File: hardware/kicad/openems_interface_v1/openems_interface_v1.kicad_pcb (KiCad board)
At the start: 2 copper layers, 130 x 100 mm, 0 parts

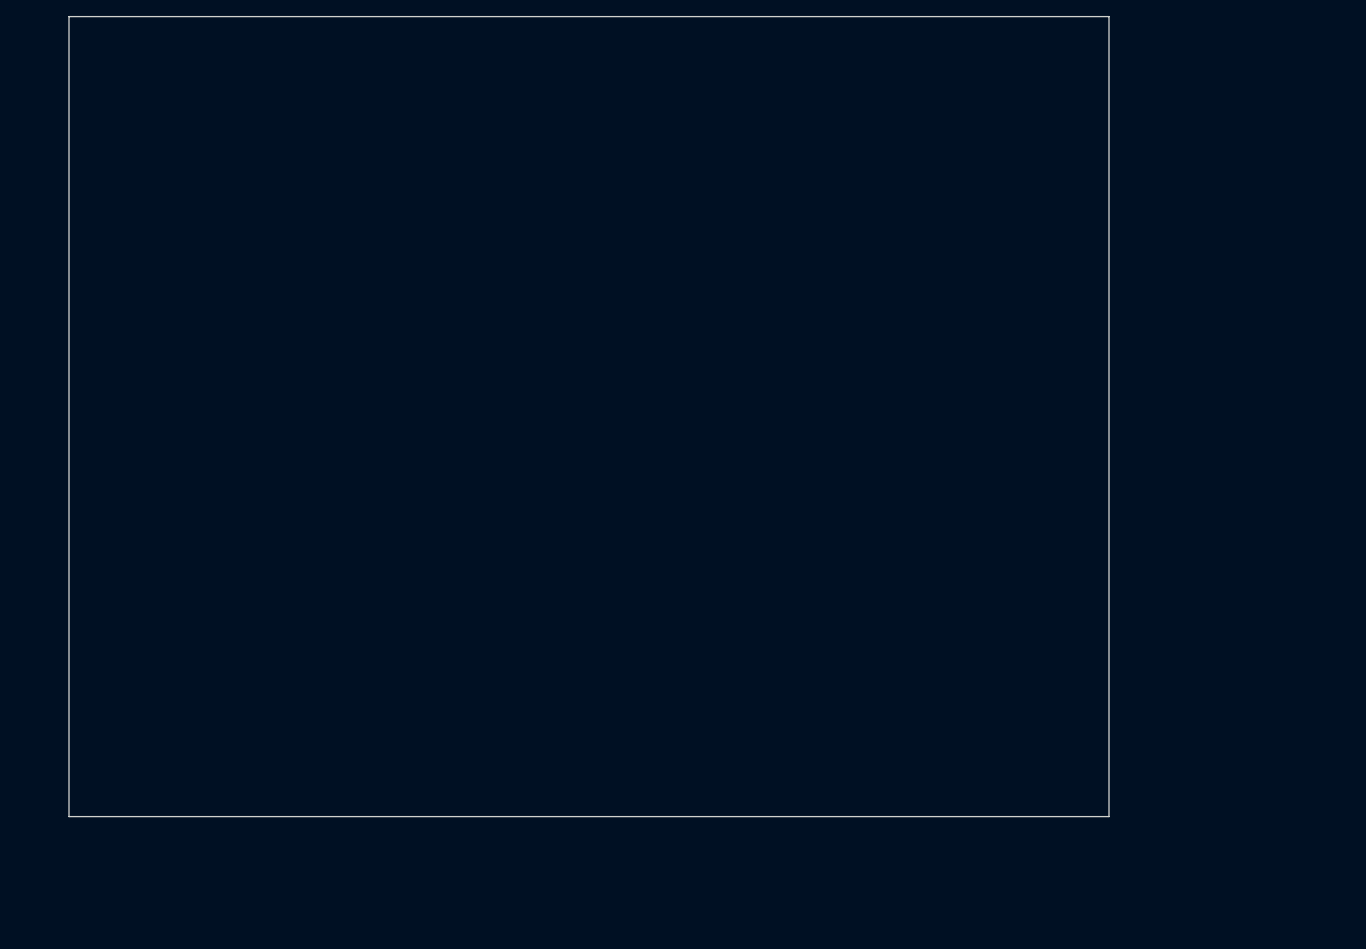
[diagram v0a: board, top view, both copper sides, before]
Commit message: feat(hw): PCB placement AMPSEAL J1/J2 + WeAct keepout
Coloca footprints TE 35/23 RA na aresta, headers 2x25 e furos M3 Φ3.2
do coreboard WeAct num outline 130x100 mm. Script build_pcb_placement.py
regenera a posição.
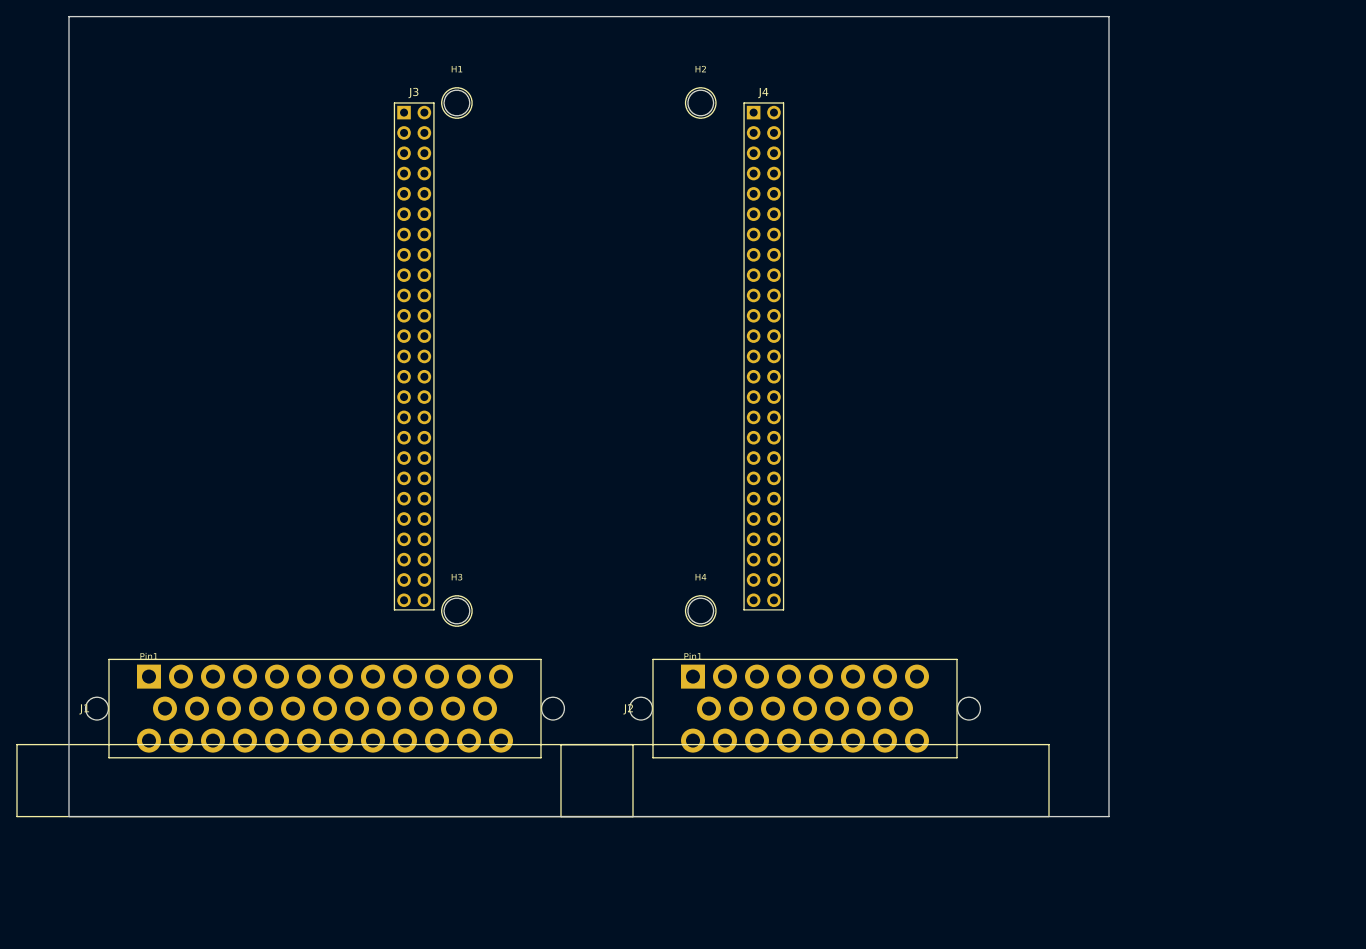
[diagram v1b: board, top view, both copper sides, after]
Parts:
- added H1: MH3.2, MountingHole:3.2mm, F.Cu at (48.5, 10.8)
- added H2: MH3.2, MountingHole:3.2mm, F.Cu at (79.0, 10.8)
- added H3: MH3.2, MountingHole:3.2mm, F.Cu at (48.5, 74.3)
- added H4: MH3.2, MountingHole:3.2mm, F.Cu at (79.0, 74.3)
- added J1: TE_776180_AMPSEAL_35_RA, OpenEMS:TE_776180_AMPSEAL_35_RA, F.Cu at (10.0, 82.5)
- added J2: TE_770669_AMPSEAL_23_RA, OpenEMS:TE_770669_AMPSEAL_23_RA, F.Cu at (78.0, 82.5)
- added J3: WeAct_PinHeader_2x25_P2.54mm, OpenEMS:WeAct_PinHeader_2x25_P2.54mm, F.Cu at (43.1, 12.0)
- added J4: WeAct_PinHeader_2x25_P2.54mm, OpenEMS:WeAct_PinHeader_2x25_P2.54mm, F.Cu at (86.9, 12.0)
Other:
- board text added: "J1 signals 1-776180-1"
- board text added: "J2 power 1-770669-1"
- board text added: "OpenEMS interface v1 — 130x100 mm\nBottom: J1 35 + J2 23 AMPSEAL RA\nCenter: WeAct 38.62x69.10 + MH Phi3.2\nNAO fabricar sem copper/GND pours"
- board text added: "WeAct keepout"
- board text removed: "J1 35-pos signals (1-776180-1)"
- board text removed: "J2 23-pos power (1-770669-1)"
- board text removed: "OpenEMS interface v1 — 130x100 mm outline Bottom edge: J1 AMPSEAL35 + gap + J2 AMPSEAL23 Center: WeAct 38.62x69.10 keepout Footprints: libs/OpenEMS.pretty — NAO fabricar ainda"
- board text removed: "WeAct keepout 38.62 x 69.10"

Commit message: feat(hw): nets J1/J2 no PCB + zones PGND + star GND no sch
Atribui pads AMPSEAL a partir de pinmap_logical.md (autoridade),
adiciona pours PGND F/B, e evita curto de terras no esquemático
(star só via NetTie no layout). Script annotate_pcb_nets.py.
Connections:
- J1 pad 1: (no net) -> CKP_P
- J1 pad 10: (no net) -> APP1
- J1 pad 11: (no net) -> APP2
- J1 pad 12: (no net) -> FUEL_PRESS
- J1 pad 13: (no net) -> OIL_PRESS
- J1 pad 14: (no net) -> ETB_TPS1
- J1 pad 15: (no net) -> ETB_TPS2
- J1 pad 16: (no net) -> +5V_SENS_A
- J1 pad 17: (no net) -> +5V_SENS_B
- J1 pad 18: (no net) -> SGND
- J1 pad 19: (no net) -> SGND
- J1 pad 2: (no net) -> CKP_N
- J1 pad 20: (no net) -> CANH
- J1 pad 21: (no net) -> CANL
- J1 pad 22: (no net) -> CAN_SHLD
- J1 pad 23: (no net) -> FLEX_12V
- J1 pad 24: (no net) -> FLEX_SIG
- J1 pad 25: (no net) -> FLEX_GND
- J1 pad 26: (no net) -> KNOCK_SIG
- J1 pad 27: (no net) -> KNOCK_SHLD
- J1 pad 28: (no net) -> CMP2_SIG
- J1 pad 29: (no net) -> CMP2_5V
- J1 pad 3: (no net) -> CKP_SHLD
- J1 pad 30: (no net) -> CMP2_GND
- J1 pad 31: (no net) -> TPS_INDEP
- J1 pad 4: (no net) -> CMP_SIG
- J1 pad 5: (no net) -> CMP_5V
- J1 pad 6: (no net) -> CMP_GND
- J1 pad 7: (no net) -> MAP
- J1 pad 8: (no net) -> CLT
- J1 pad 9: (no net) -> IAT
- J2 pad 1: (no net) -> VBAT_RAW
- J2 pad 10: (no net) -> IGN1
- J2 pad 11: (no net) -> IGN2
- J2 pad 12: (no net) -> IGN3
- J2 pad 13: (no net) -> IGN4
- J2 pad 14: (no net) -> VVT_EXH
- J2 pad 15: (no net) -> VVT_INT
- J2 pad 16: (no net) -> PUMP_RLY
- J2 pad 17: (no net) -> FAN_RLY
- J2 pad 18: (no net) -> MAIN_RLY
- J2 pad 19: (no net) -> ETB_MOTOR_P
- J2 pad 2: (no net) -> VBAT_RAW
- J2 pad 20: (no net) -> ETB_MOTOR_P
- J2 pad 21: (no net) -> ETB_MOTOR_N
- J2 pad 22: (no net) -> ETB_MOTOR_N
- J2 pad 3: (no net) -> PGND
- J2 pad 4: (no net) -> PGND
- J2 pad 5: (no net) -> PGND
- J2 pad 6: (no net) -> INJ1
- J2 pad 7: (no net) -> INJ2
- J2 pad 8: (no net) -> INJ3
- J2 pad 9: (no net) -> INJ4
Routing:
- added copper zone on B.Cu, net PGND
- added copper zone on F.Cu, net PGND
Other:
- board text added: "PGND zones F+B (B: Fill All Zones in Pcbnew) J1/J2 nets = pinmap_logical.md (authoritative) Star NetTie: PGND-SGND-AGND-SHIELD near WeAct AGND pour island near ADC later"

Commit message: feat(hw): integrar footprints rusEFI AMPSEAL 35 + NetTie star
Revisão Speeduino/rusEFI KiCad libs: J1 passa a usar AMPSEAL_35 RA do
rusEFI (776180), pads 2.45 mm alinhados, NetTie-4 no star GND. Doc em
kicad_vendor_review.md; clones upstream em vendor/ (gitignore).
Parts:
- added NT1: NetTie-4_THT_Pad1.0mm, OpenEMS:NetTie-4_THT_Pad1.0mm, F.Cu at (37.7, 10.0)
- J1: value TE_776180_AMPSEAL_35_RA -> rusEFI_AMPSEAL_35_RA_776180; footprint OpenEMS:TE_776180_AMPSEAL_35_RA -> OpenEMS:rusEFI_AMPSEAL_35_RA_776180
- moved J1 22.4 mm to (32.0, 86.5)

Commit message: feat(hw): routing potência VBAT/PGND + corredores CKP/SPI
Trilhas grossas VBAT_RAW e PGND (J2→NetTie/star), stubs ETB/INJ/IGN,
par CKP afastado da potência, keepouts Eco1. Script route_power.py
integrado no placement.
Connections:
- J1 pad 22: CAN_SHLD -> SHIELD_GND
- J1 pad 27: KNOCK_SHLD -> SHIELD_GND
- J1 pad 3: CKP_SHLD -> SHIELD_GND
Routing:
- net PGND: track 0.00 -> 255.3 mm, vias 0 -> 2
- net SHIELD_GND: track 0.00 -> 92.2 mm, vias 0 -> 1
- net CKP_P: track 0.00 -> 47.5 mm
- net CKP_N: track 0.00 -> 45.5 mm
- net VBAT_RAW: track 0.00 -> 33.7 mm, vias 0 -> 1
- net ETB_MOTOR_N: track 0.00 -> 18.5 mm
- net ETB_MOTOR_P: track 0.00 -> 16.5 mm
- net INJ4: track 0.00 -> 14.5 mm
- net IGN4: track 0.00 -> 12.5 mm
- net IGN3: track 0.00 -> 12.5 mm
- net IGN2: track 0.00 -> 12.5 mm
- net IGN1: track 0.00 -> 12.5 mm
- net INJ3: track 0.00 -> 10.5 mm
- net INJ2: track 0.00 -> 10.5 mm
- net INJ1: track 0.00 -> 10.5 mm
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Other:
- board text added: "CKP quiet no INJ/ETB"
- board text added: "PWR bay FET/fuse/bulk"
- board text added: "Routing: VBAT_RAW/PGND thick; ETB dual; CKP pair N; SPI keepout Fill zones after open. TLE/power parts not placed yet — stubs only."
- board text added: "SPI2 corridor PB12-15 ↔ TLE"
- board text added: "TLE power zone (BAT/OUT stubs)"

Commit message: feat(hw): colocar TLE8888 LQFP-100 e power stage no PCB
U3 + Q1 reverse FET, F1, TVS, bulk, buck SOT-23-6; nets TLE (SPI,
BAT/PGND, INJ/IGN A+B, straps); ligações a J2 stubs e corredor CKP/SPI.
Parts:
- added C1: CP_Elec_6.3x5.8, OpenEMS:CP_Elec_6.3x5.8, F.Cu at (78.0, 70.0)
- added C2: C_0805_2012Metric, OpenEMS:C_0805_2012Metric, F.Cu at (83.0, 70.0)
- added D1: D_SMB, OpenEMS:D_SMB, F.Cu at (70.0, 76.0)
- added F1: Fuse_1206_3216Metric, OpenEMS:Fuse_1206_3216Metric, F.Cu at (70.0, 70.0)
- added Q1: SOT-23, OpenEMS:SOT-23, F.Cu at (62.0, 70.0)
- added U1: SOT-23-6, OpenEMS:SOT-23-6, F.Cu at (62.0, 58.0)
- added U3: LQFP-100_14x14mm_P0.5mm, OpenEMS:LQFP-100_14x14mm_P0.5mm, F.Cu at (92.0, 52.0)
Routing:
- net VBAT: track 0.00 -> 116.6 mm
- net CKP_P: track 47.5 -> 134.0 mm
- net CKP_N: track 45.5 -> 130.1 mm
- net IGN4: track 12.5 -> 61.9 mm
- net IGN3: track 12.5 -> 58.4 mm
- net IGN2: track 12.5 -> 55.1 mm
- net IGN1: track 12.5 -> 52.0 mm
- net INJ4: track 14.5 -> 38.4 mm
- net INJ3: track 10.5 -> 32.0 mm
- net MCU_PB13: track 0.00 -> 21.4 mm
- net MCU_PB15: track 0.00 -> 20.9 mm
- net MCU_PB14: track 0.00 -> 20.6 mm
- net MCU_PB12: track 0.00 -> 20.4 mm
- net INJ2: track 10.5 -> 30.1 mm
- net INJ1: track 10.5 -> 29.1 mm
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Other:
- board text added: "Power stage: Q1→F1→VBAT bulk→TLE BAT; buck→+5V_MAIN TLE U3 LQFP100 @ (92,52). Straps SIN=AGND FCLN=+3V3 on copper."

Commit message: feat(hw): fechar scaffold PCB — LDO, WeAct nets, SPI/CAN/drive
Pipeline build_all: LDO 3V3+FB VDDA, anotar J3/J4, cobre SPI/CAN e
direct-drive WeAct↔TLE. ~127 segments; não fabricar sem DRC manual.
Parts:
- added C3: C_0805_2012Metric, OpenEMS:C_0805_2012Metric, F.Cu at (50.0, 52.0)
- added C4: C_0805_2012Metric, OpenEMS:C_0805_2012Metric, F.Cu at (50.0, 58.0)
- added FB1: L_0805_2012Metric, OpenEMS:L_0805_2012Metric, F.Cu at (55.0, 52.0)
- added U2: SOT-23-5, OpenEMS:SOT-23-5, F.Cu at (55.0, 58.0)
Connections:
- J3 pad 1: (no net) -> MCU_PC0
- J3 pad 10: (no net) -> MCU_PA3
- J3 pad 11: (no net) -> MCU_PA4
- J3 pad 12: (no net) -> MCU_PA5
- J3 pad 15: (no net) -> MCU_PC4
- J3 pad 16: (no net) -> MCU_PC5
- J3 pad 17: (no net) -> MCU_PB0
- J3 pad 18: (no net) -> MCU_PB1
- J3 pad 2: (no net) -> MCU_PC1
- J3 pad 20: (no net) -> MCU_PE7
- J3 pad 21: (no net) -> MCU_PE8
- J3 pad 22: (no net) -> MCU_PE9
- J3 pad 23: (no net) -> MCU_PE10
- J3 pad 24: (no net) -> MCU_PE11
- J3 pad 25: (no net) -> MCU_PE12
- J3 pad 26: (no net) -> MCU_PE13
- J3 pad 29: (no net) -> MCU_PB12
- J3 pad 3: (no net) -> MCU_PC2
- J3 pad 30: (no net) -> MCU_PB13
- J3 pad 31: (no net) -> MCU_PB14
- J3 pad 32: (no net) -> MCU_PB15
- J3 pad 4: (no net) -> MCU_PC3
- J3 pad 5: (no net) -> AGND
- J3 pad 6: (no net) -> VREF_P
- J3 pad 7: (no net) -> MCU_PA0
- J3 pad 8: (no net) -> MCU_PA1
- J3 pad 9: (no net) -> MCU_PA2
- J4 pad 1: (no net) -> VB_WEACT
- J4 pad 10: (no net) -> MCU_PB9
- J4 pad 11: (no net) -> MCU_PB6
- J4 pad 12: (no net) -> MCU_PB7
- J4 pad 2: (no net) -> MCU_PE6
- J4 pad 28: (no net) -> MCU_PA11
- J4 pad 3: (no net) -> MCU_PE4
- J4 pad 30: (no net) -> MCU_PA12
- J4 pad 4: (no net) -> MCU_PE5
- J4 pad 5: (no net) -> MCU_PE2
- J4 pad 6: (no net) -> MCU_PE3
- J4 pad 7: (no net) -> MCU_PE0
- J4 pad 9: (no net) -> MCU_PB8
- U3 pad 21: CKP_DIG -> MCU_PA0
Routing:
- net MCU_PA0: track 0.00 -> 157.7 mm, vias 0 -> 1
- net +3V3: track 0.00 -> 88.4 mm, vias 2 -> 3
- net MCU_PE10: track 0.00 -> 68.9 mm
- net MCU_PE9: track 0.00 -> 66.9 mm
- net MCU_PE12: track 0.00 -> 66.8 mm
- net MCU_PE11: track 0.00 -> 64.8 mm
- net MCU_PE13: track 0.00 -> 62.8 mm
- net MCU_PE6: track 0.00 -> 48.1 mm
- net MCU_PE4: track 0.00 -> 47.6 mm
- net MCU_PB8: track 0.00 -> 46.4 mm
- net MCU_PE2: track 0.00 -> 44.5 mm
- net MCU_PB9: track 0.00 -> 44.4 mm
- net MCU_PE3: track 0.00 -> 44.2 mm
- net MCU_PE0: track 0.00 -> 41.5 mm
- net MCU_PB6: track 0.00 -> 41.4 mm
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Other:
- board text added: "Finish: LDO U2 + FB1 VDDA; WeAct J3/J4 nets; SPI/CAN/drive Confirm WeAct pin1 silk vs SchDoc before fab. Not production-ready."
